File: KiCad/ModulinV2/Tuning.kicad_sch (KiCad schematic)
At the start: 27 parts, among them IC50 TL074HIDR

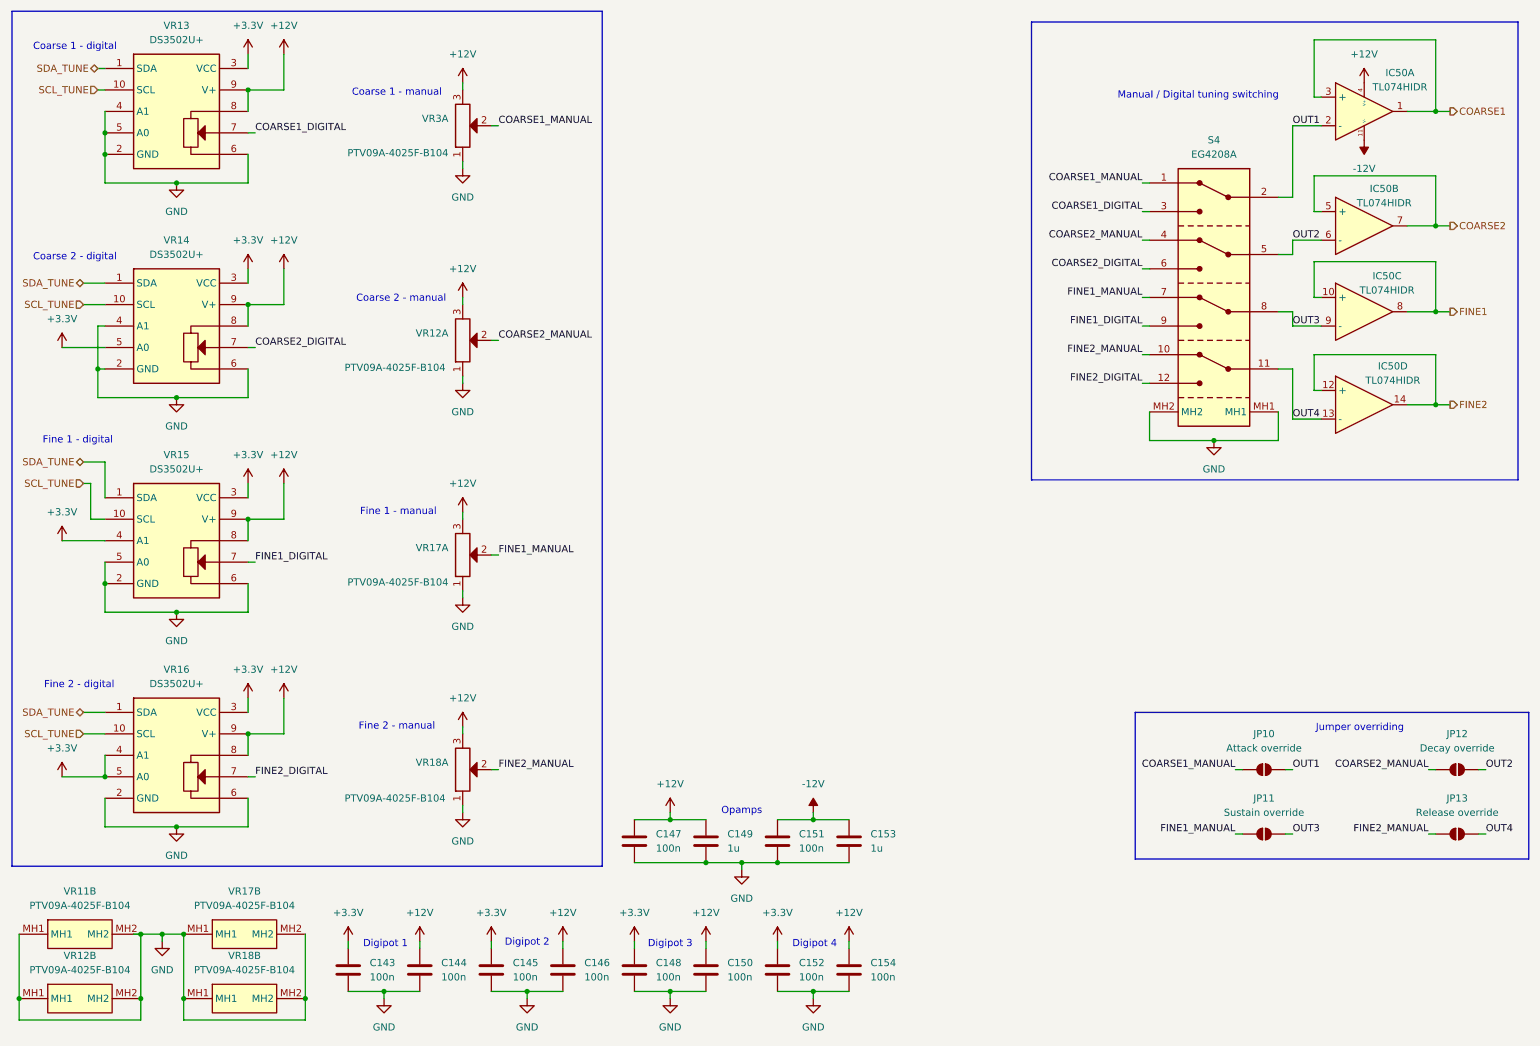
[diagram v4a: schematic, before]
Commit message: Started adding footprints for capacitors
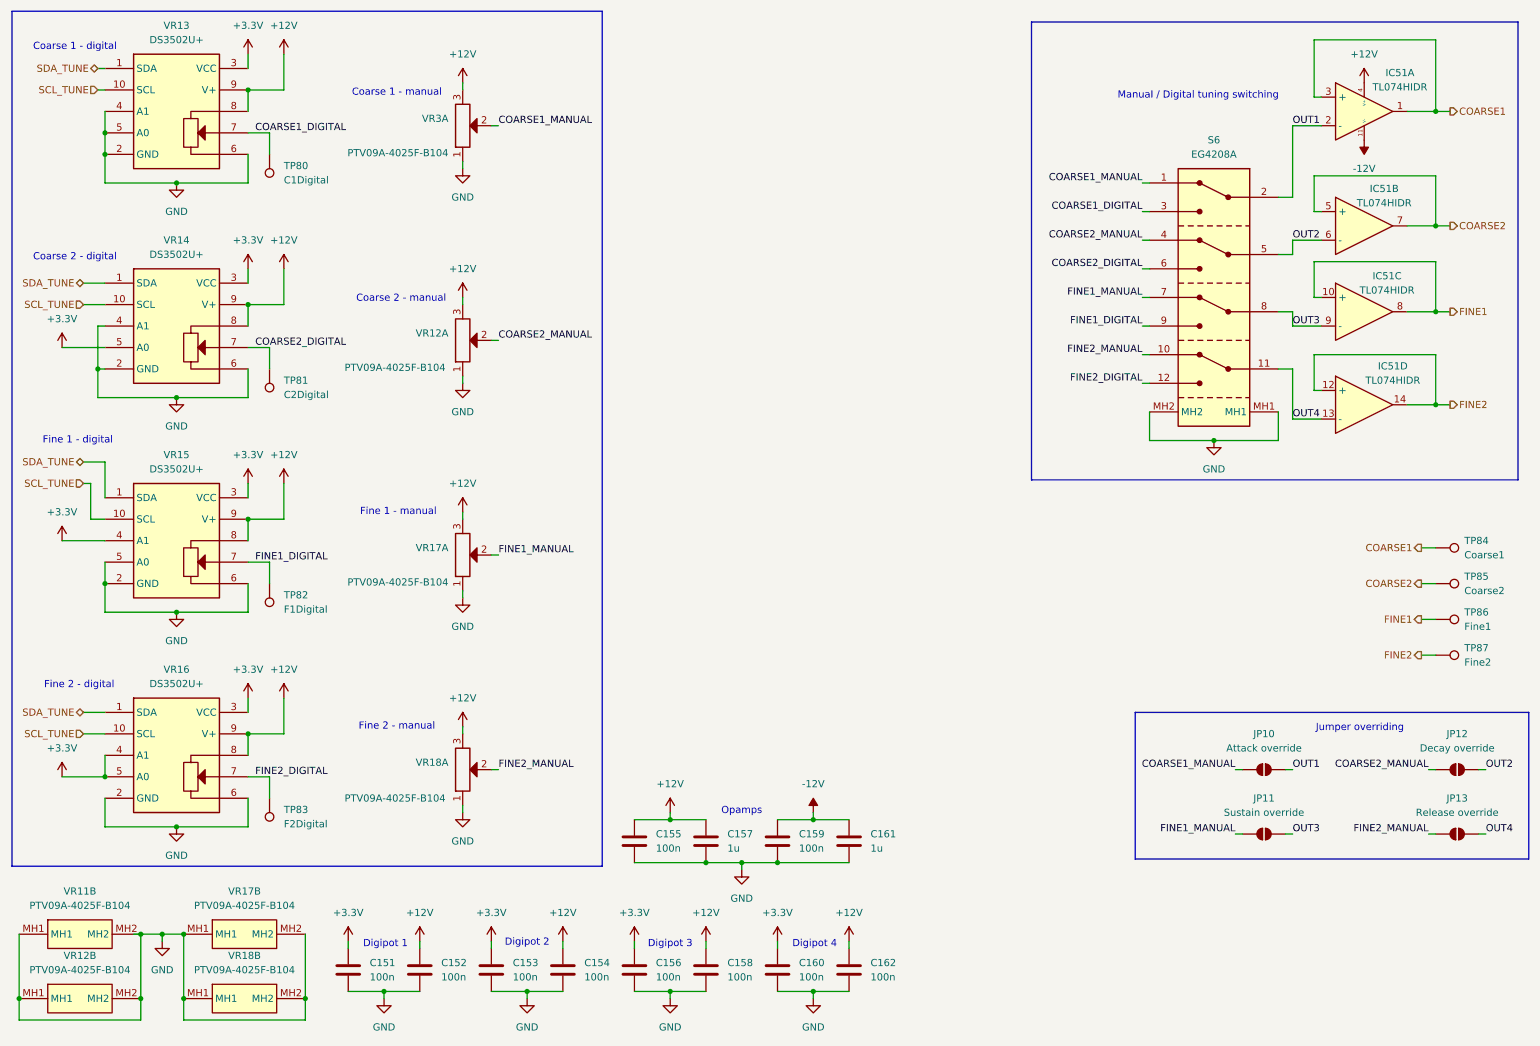
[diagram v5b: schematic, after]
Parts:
- added TP80: C1Digital, SamacSys_Parts:TestPointLoop, symbol Connector:TestPoint
- added TP81: C2Digital, SamacSys_Parts:TestPointLoop, symbol Connector:TestPoint
- added TP82: F1Digital, SamacSys_Parts:TestPointLoop, symbol Connector:TestPoint
- added TP83: F2Digital, SamacSys_Parts:TestPointLoop, symbol Connector:TestPoint
- added TP84: Coarse1, SamacSys_Parts:TestPointLoop, symbol Connector:TestPoint
- added TP85: Coarse2, SamacSys_Parts:TestPointLoop, symbol Connector:TestPoint
- added TP86: Fine1, SamacSys_Parts:TestPointLoop, symbol Connector:TestPoint
- added TP87: Fine2, SamacSys_Parts:TestPointLoop, symbol Connector:TestPoint
- C151: renamed from C143; footprint (none) -> SamacSys_Parts:CAPC1608X90N
- C152: renamed from C144; footprint (none) -> SamacSys_Parts:CAPC1608X90N
- C153: renamed from C145; footprint (none) -> SamacSys_Parts:CAPC1608X90N
- C154: renamed from C146; footprint (none) -> SamacSys_Parts:CAPC1608X90N
- C155: renamed from C147; footprint (none) -> SamacSys_Parts:CAPC1608X90N
- C156: renamed from C148; footprint (none) -> SamacSys_Parts:CAPC1608X90N
- C157: renamed from C149; footprint (none) -> SamacSys_Parts:CAPC1608X95N
- C158: renamed from C150; footprint (none) -> SamacSys_Parts:CAPC1608X90N
- C159: renamed from C151; footprint (none) -> SamacSys_Parts:CAPC1608X90N
- C160: renamed from C152; footprint (none) -> SamacSys_Parts:CAPC1608X90N
- C161: renamed from C153; footprint (none) -> SamacSys_Parts:CAPC1608X95N
- C162: renamed from C154; footprint (none) -> SamacSys_Parts:CAPC1608X90N
- renumbered IC50 to IC51, S4 to S6
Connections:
- net COARSE1: now also TP84.1
- net COARSE1_DIGITAL: now also TP80.1
- net COARSE2: now also TP85.1
- net COARSE2_DIGITAL: now also TP81.1
- net FINE1: now also TP86.1
- net FINE1_DIGITAL: now also TP82.1
- net FINE2: now also TP87.1
- net FINE2_DIGITAL: now also TP83.1

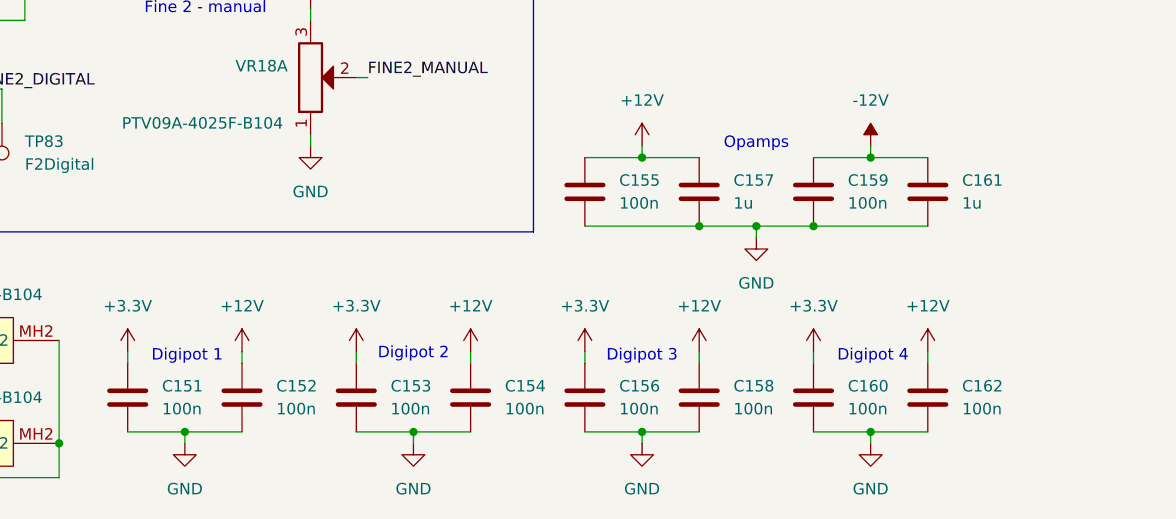
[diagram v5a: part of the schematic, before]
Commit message: Added footprints to all capacitors and potentiometers
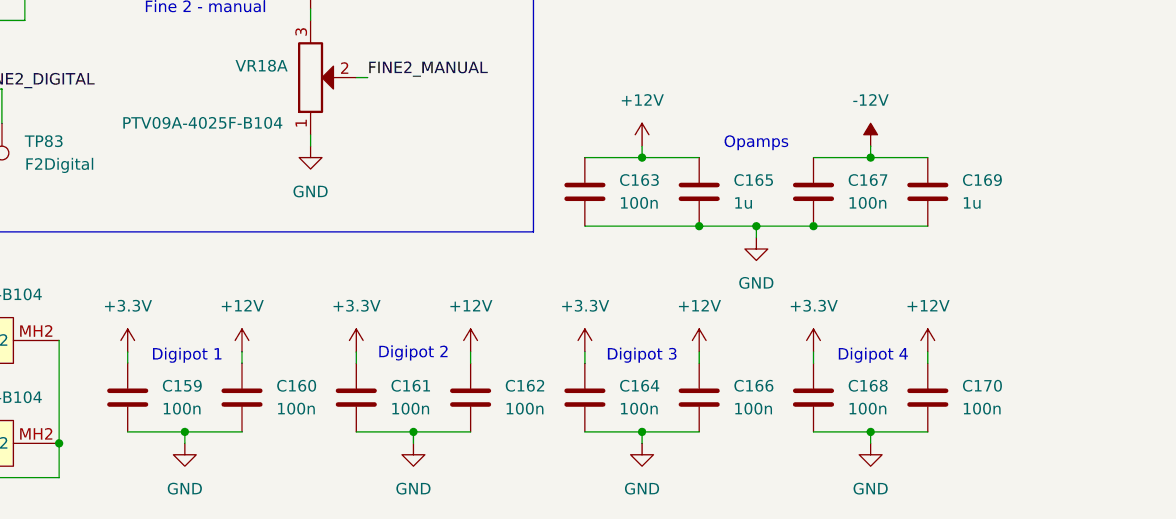
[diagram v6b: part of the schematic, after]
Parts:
- C159: renamed from C151; footprint SamacSys_Parts:CAPC1608X90N -> Capacitor_SMD:C_0603_1608Metric_Pad1.08x0.95mm_HandSolder
- C160: renamed from C152; footprint SamacSys_Parts:CAPC1608X90N -> Capacitor_SMD:C_0603_1608Metric_Pad1.08x0.95mm_HandSolder
- C161: renamed from C153; footprint SamacSys_Parts:CAPC1608X90N -> Capacitor_SMD:C_0603_1608Metric_Pad1.08x0.95mm_HandSolder
- C162: renamed from C154; footprint SamacSys_Parts:CAPC1608X90N -> Capacitor_SMD:C_0603_1608Metric_Pad1.08x0.95mm_HandSolder
- C163: renamed from C155; footprint SamacSys_Parts:CAPC1608X90N -> Capacitor_SMD:C_0603_1608Metric_Pad1.08x0.95mm_HandSolder
- C164: renamed from C156; footprint SamacSys_Parts:CAPC1608X90N -> Capacitor_SMD:C_0603_1608Metric_Pad1.08x0.95mm_HandSolder
- C165: renamed from C157; footprint SamacSys_Parts:CAPC1608X95N -> Capacitor_SMD:C_0603_1608Metric_Pad1.08x0.95mm_HandSolder
- C166: renamed from C158; footprint SamacSys_Parts:CAPC1608X90N -> Capacitor_SMD:C_0603_1608Metric_Pad1.08x0.95mm_HandSolder
- C167: renamed from C159; footprint SamacSys_Parts:CAPC1608X90N -> Capacitor_SMD:C_0603_1608Metric_Pad1.08x0.95mm_HandSolder
- C168: renamed from C160; footprint SamacSys_Parts:CAPC1608X90N -> Capacitor_SMD:C_0603_1608Metric_Pad1.08x0.95mm_HandSolder
- C169: renamed from C161; footprint SamacSys_Parts:CAPC1608X95N -> Capacitor_SMD:C_0603_1608Metric_Pad1.08x0.95mm_HandSolder
- C170: renamed from C162; footprint SamacSys_Parts:CAPC1608X90N -> Capacitor_SMD:C_0603_1608Metric_Pad1.08x0.95mm_HandSolder

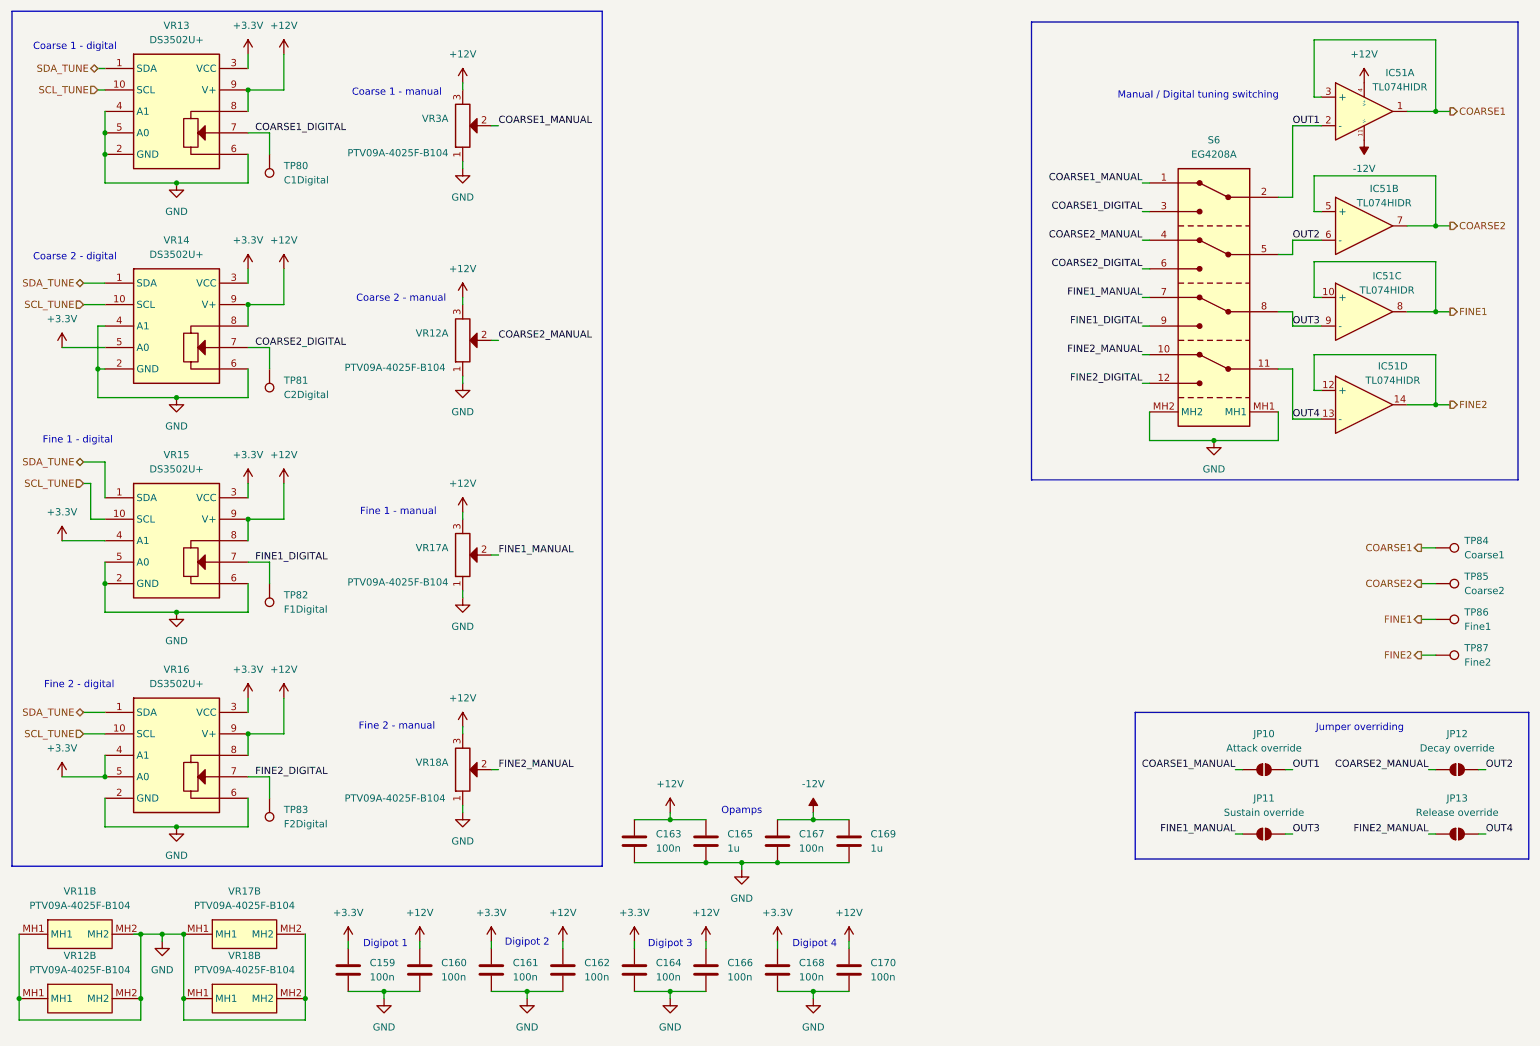
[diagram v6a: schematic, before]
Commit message: Finished Schematic, started on PCB
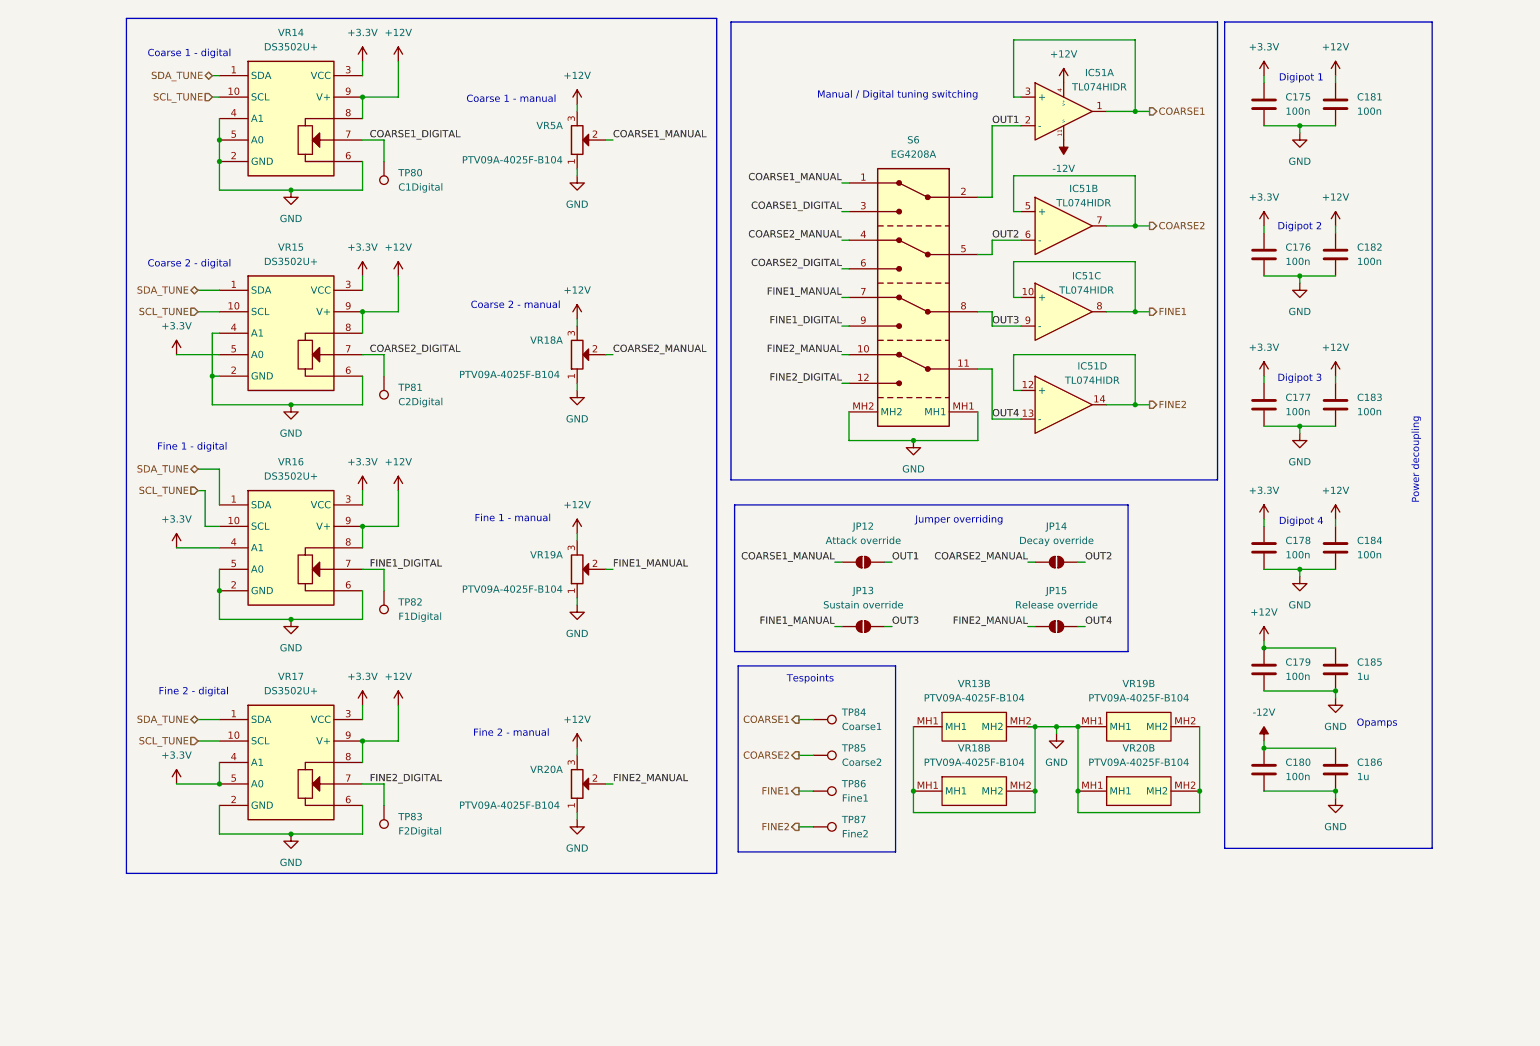
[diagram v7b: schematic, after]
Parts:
- renumbered C159 to C175, C161 to C176, C164 to C177, C168 to C178, C163 to C179, C167 to C180, C160 to C181, C162 to C182, C166 to C183, C170 to C184, C165 to C185, C169 to C186, JP10 to JP12, JP11 to JP13, JP12 to JP14, JP13 to JP15, VR11 to VR13, VR13 to VR14, VR14 to VR15, VR15 to VR16, VR16 to VR17, VR12 to VR18, VR17 to VR19, VR18 to VR20, VR3 to VR5
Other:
- note added: "Power decoupling"
- note added: "Tespoints"
- moved on the sheet: C175, C176, C177, C178, C179, C180, C181, C182, C183, C184, C185, C186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
